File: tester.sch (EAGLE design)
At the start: 72 parts, among them IC1 ATmega8/88/168, K1 NA 05W K, M1 SP6000C-180, P1 250, P2 10k lin, Q1 BC847CSMD, Q2 BC847CSMD, Q3 BC328-40, Q4 8,000 MHz, Q5 BC847CSMD, Q9 IRFR9024, U1 LT1004CZ-2.5, U2 MCP1702-5002, U3 MCP1702-5002, U4 LM339D, U5 BCR421U, X1 NEB21R

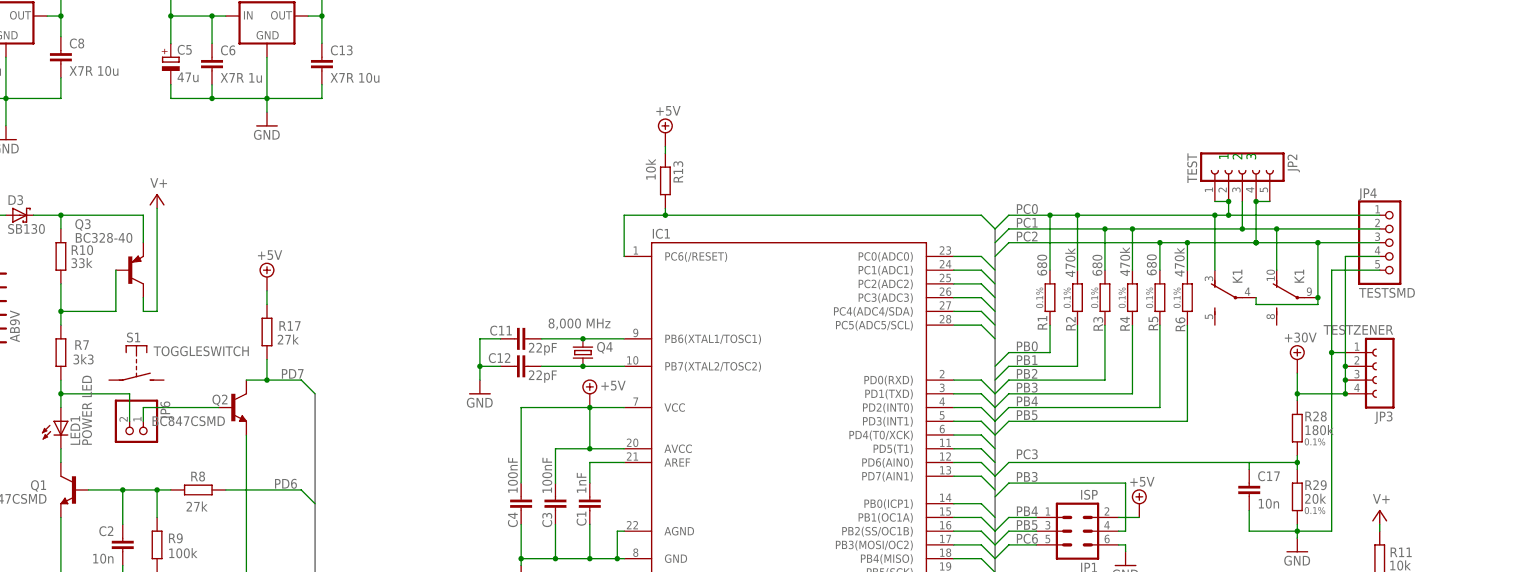
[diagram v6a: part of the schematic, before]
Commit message: rearranged top mask
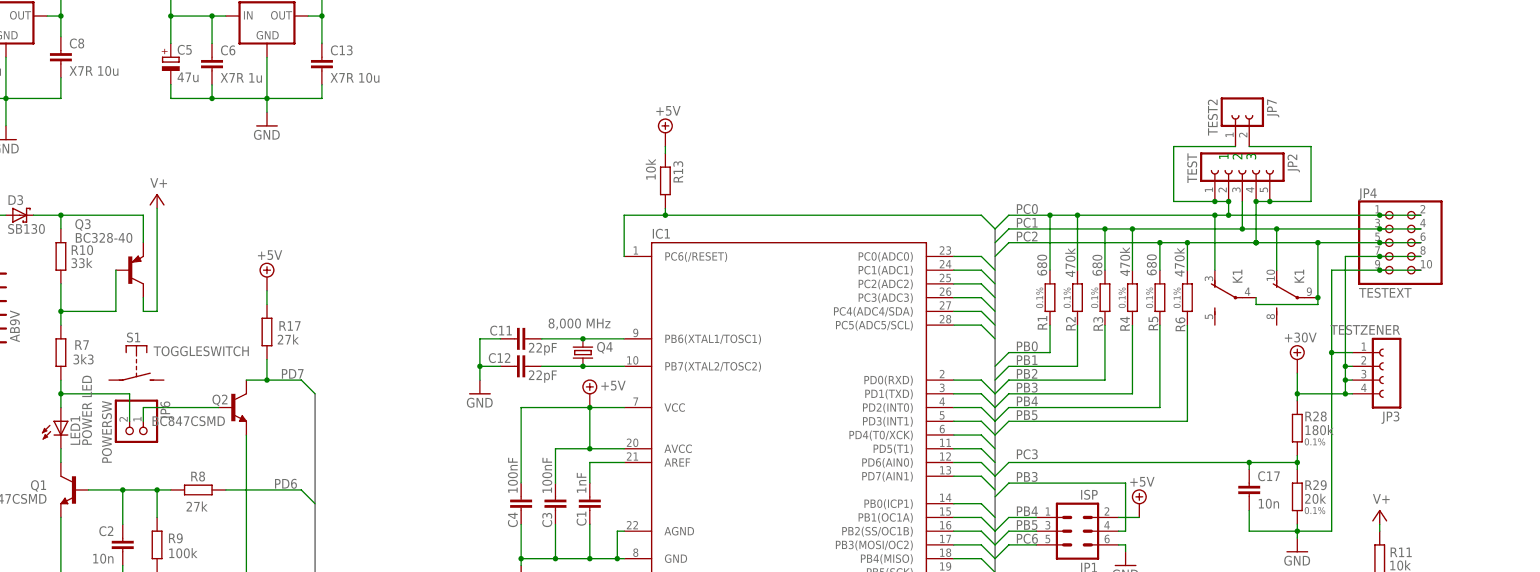
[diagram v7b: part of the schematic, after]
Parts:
- added JP7: TEST2, con-lsta:FE02-1
- JP4: value TESTSMD -> TESTEXT; device pinhead:PINHD-1X5 -> pinhead:PINHD-2X5
- JP6: value (none) -> POWERSW
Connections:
- net +30V: now also JP4.7, JP4.8; no longer JP4.4
- net GND: now also JP4.10, JP4.9; no longer JP4.5
- net PC0: now also JP4.2, JP7.1
- net PC1: now also JP4.3, JP4.4; no longer JP4.2
- net PC2: now also JP4.5, JP4.6, JP7.2; no longer JP4.3
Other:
- moved on the sheet: JP3
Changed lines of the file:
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@@
 <setting verticaltext="up"/>
 </settings>
-<grid distance="0.1" unitdist="inch" unit="mm" style="lines" multiple="1" display="yes" altdistance="0.01" altunitdist="inch" altunit="mm"/>
+<grid distance="1.27" unitdist="mm" unit="mm" style="lines" multiple="1" display="yes" altdistance="635" altunitdist="mic" altunit="mic"/>
 <layers>
 <layer number="1" name="Top" color="4" fill="1" visible="no" active="no"/>
@@
 <part name="R16" library="resistor" deviceset="R-EU_" device="R0603" value="2k2"/>
 <part name="U1" library="reference" deviceset="LM329*" device="Z" technology="D" value="LT1004CZ-2.5"/>
-<part name="JP4" library="pinhead" deviceset="PINHD-1X5" device="" value="TESTSMD">
+<part name="JP4" library="pinhead" deviceset="PINHD-2X5" device="" value="TESTEXT">
 <attribute name="REICHELT" value="AW 226/20"/>
 </part>
@@
 <part name="M1" library="strapubox" deviceset="SP6000" device="C-180" value="SP6000C-180"/>
 <part name="S1" library="external" deviceset="TOGGLESWITCH" device=""/>
-<part name="JP6" library="pinhead" deviceset="PINHD-1X2" device=""/>
+<part name="JP6" library="pinhead" deviceset="PINHD-1X2" device="" value="POWERSW"/>
 <part name="PLATINENSAMMLER" library="Platinensammler" deviceset="LP_NUMBER" device="08_SILK_TOP"/>
+<part name="JP7" library="con-lsta" deviceset="FE02-1" device="" value="TEST2"/>
 </parts>
 <sheets>
@@
 <instance part="SUPPLY2" gate="+24V" x="294.64" y="181.61"/>
 <instance part="GND7" gate="1" x="294.64" y="146.05"/>
-<instance part="JP3" gate="G$1" x="311.15" y="179.07" rot="R180"/>
+<instance part="JP3" gate="G$1" x="312.42" y="179.07" rot="R180"/>
 <instance part="D1" gate="G$1" x="288.29" y="101.6" rot="R90"/>
 <instance part="U5" gate="G$1" x="129.54" y="66.04"/>
@@
 <instance part="JP6" gate="G$1" x="78.74" y="167.64" rot="R270"/>
 <instance part="PLATINENSAMMLER" gate="G$1" x="351.79" y="248.92"/>
+<instance part="JP7" gate="G$1" x="284.48" y="228.6" rot="R270"/>
 </instances>
 <busses>
@@
 <wire x1="300.99" y1="149.86" x2="300.99" y2="182.88" width="0.1524" layer="91"/>
 <pinref part="JP3" gate="G$1" pin="1"/>
-<wire x1="300.99" y1="182.88" x2="303.53" y2="182.88" width="0.1524" layer="91"/>
+<wire x1="300.99" y1="182.88" x2="304.8" y2="182.88" width="0.1524" layer="91"/>
 <junction x="300.99" y="182.88"/>
-<pinref part="JP4" gate="A" pin="5"/>
+<pinref part="JP4" gate="A" pin="9"/>
 <wire x1="309.88" y1="198.12" x2="300.99" y2="198.12" width="0.1524" layer="91"/>
 <wire x1="300.99" y1="198.12" x2="300.99" y2="182.88" width="0.1524" layer="91"/>
+<pinref part="JP4" gate="A" pin="10"/>
+<wire x1="317.5" y1="198.12" x2="309.88" y2="198.12" width="0.1524" layer="91"/>
+<junction x="309.88" y="198.12"/>
 </segment>
 <segment>
@@
 <wire x1="279.4" y1="198.12" x2="279.4" y2="208.28" width="0.1524" layer="91"/>
 <junction x="279.4" y="208.28"/>
+<wire x1="279.4" y1="210.82" x2="271.78" y2="210.82" width="0.1524" layer="91"/>
+<junction x="279.4" y="210.82"/>
+<wire x1="271.78" y1="210.82" x2="271.78" y2="220.98" width="0.1524" layer="91"/>
+<pinref part="JP4" gate="A" pin="2"/>
+<wire x1="309.88" y1="208.28" x2="317.5" y2="208.28" width="0.1524" layer="91"/>
+<junction x="309.88" y="208.28"/>
+<pinref part="JP7" gate="G$1" pin="1"/>
+<wire x1="271.78" y1="220.98" x2="283.21" y2="220.98" width="0.1524" layer="91"/>
 </segment>
 </net>
@@
 <pinref part="JP2" gate="G$1" pin="3"/>
 <wire x1="284.48" y1="205.74" x2="284.48" y2="210.82" width="0.1524" layer="91"/>
-<pinref part="JP4" gate="A" pin="2"/>
+<pinref part="JP4" gate="A" pin="3"/>
 <wire x1="309.88" y1="205.74" x2="290.83" y2="205.74" width="0.1524" layer="91"/>
 <junction x="284.48" y="205.74"/>
@@
 <wire x1="290.83" y1="198.12" x2="290.83" y2="205.74" width="0.1524" layer="91"/>
 <junction x="290.83" y="205.74"/>
+<pinref part="JP4" gate="A" pin="4"/>
+<wire x1="317.5" y1="205.74" x2="309.88" y2="205.74" width="0.1524" layer="91"/>
+<junction x="309.88" y="205.74"/>
 </segment>
 </net>
@@
 <junction x="287.02" y="203.2"/>
 <junction x="287.02" y="203.2"/>
-<pinref part="JP4" gate="A" pin="3"/>
+<pinref part="JP4" gate="A" pin="5"/>
 <wire x1="309.88" y1="203.2" x2="298.45" y2="203.2" width="0.1524" layer="91"/>
 <pinref part="K1" gate="2" pin="P"/>
@@
 <junction x="298.45" y="203.2"/>
 <junction x="298.45" y="193.04"/>
+<wire x1="289.56" y1="210.82" x2="297.18" y2="210.82" width="0.1524" layer="91"/>
+<junction x="289.56" y="210.82"/>
+<wire x1="297.18" y1="210.82" x2="297.18" y2="220.98" width="0.1524" layer="91"/>
+<pinref part="JP4" gate="A" pin="6"/>
+<wire x1="317.5" y1="203.2" x2="309.88" y2="203.2" width="0.1524" layer="91"/>
+<junction x="309.88" y="203.2"/>
+<pinref part="JP7" gate="G$1" pin="2"/>
+<wire x1="285.75" y1="220.98" x2="297.18" y2="220.98" width="0.1524" layer="91"/>
 </segment>
 </net>
@@
 <junction x="294.64" y="162.56"/>
 <label x="242.57" y="163.195" size="1.778" layer="95"/>
+<junction x="285.75" y="162.56"/>
 </segment>
 </net>
@@
 <pinref part="R28" gate="G$1" pin="2"/>
 <wire x1="294.64" y1="175.26" x2="303.53" y2="175.26" width="0.1524" layer="91"/>
+<wire x1="303.53" y1="175.26" x2="304.8" y2="175.26" width="0.1524" layer="91"/>
 <wire x1="294.64" y1="173.99" x2="294.64" y2="175.26" width="0.1524" layer="91"/>
 <junction x="294.64" y="175.26"/>
 <pinref part="SUPPLY2" gate="+24V" pin="+24V"/>
 <pinref part="JP3" gate="G$1" pin="3"/>
-<wire x1="303.53" y1="175.26" x2="303.53" y2="177.8" width="0.1524" layer="91"/>
-<wire x1="303.53" y1="177.8" x2="303.53" y2="180.34" width="0.1524" layer="91"/>
-<junction x="303.53" y="177.8"/>
 <pinref part="JP3" gate="G$1" pin="2"/>
 <pinref part="JP3" gate="G$1" pin="4"/>
+<pinref part="JP4" gate="A" pin="7"/>
+<wire x1="309.88" y1="200.66" x2="303.53" y2="200.66" width="0.1524" layer="91"/>
+<pinref part="JP4" gate="A" pin="8"/>
+<wire x1="317.5" y1="200.66" x2="309.88" y2="200.66" width="0.1524" layer="91"/>
+<junction x="309.88" y="200.66"/>
+<wire x1="303.53" y1="175.26" x2="303.53" y2="177.8" width="0.1524" layer="91"/>
 <junction x="303.53" y="175.26"/>
+<wire x1="303.53" y1="177.8" x2="303.53" y2="180.34" width="0.1524" layer="91"/>
 <wire x1="303.53" y1="180.34" x2="303.53" y2="200.66" width="0.1524" layer="91"/>
-<pinref part="JP4" gate="A" pin="4"/>
-<wire x1="309.88" y1="200.66" x2="303.53" y2="200.66" width="0.1524" layer="91"/>
+<wire x1="304.8" y1="180.34" x2="303.53" y2="180.34" width="0.1524" layer="91"/>
 <junction x="303.53" y="180.34"/>
-</segment>
-</net>
+<wire x1="304.8" y1="177.8" x2="303.53" y2="177.8" width="0.1524" layer="91"/>
+<junction x="303.53" y="177.8"/>
+</segment>
+</net>

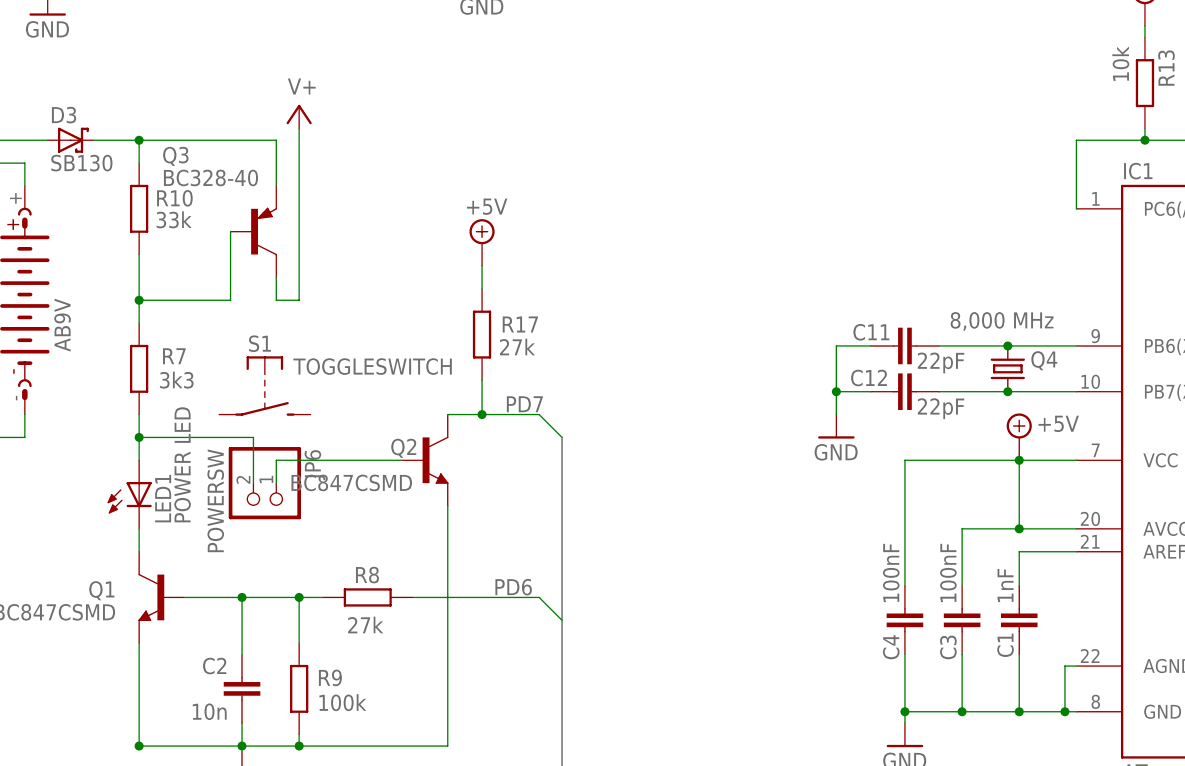
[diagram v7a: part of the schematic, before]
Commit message: cleaned up some capacitor values, changed P2 to available pinout type
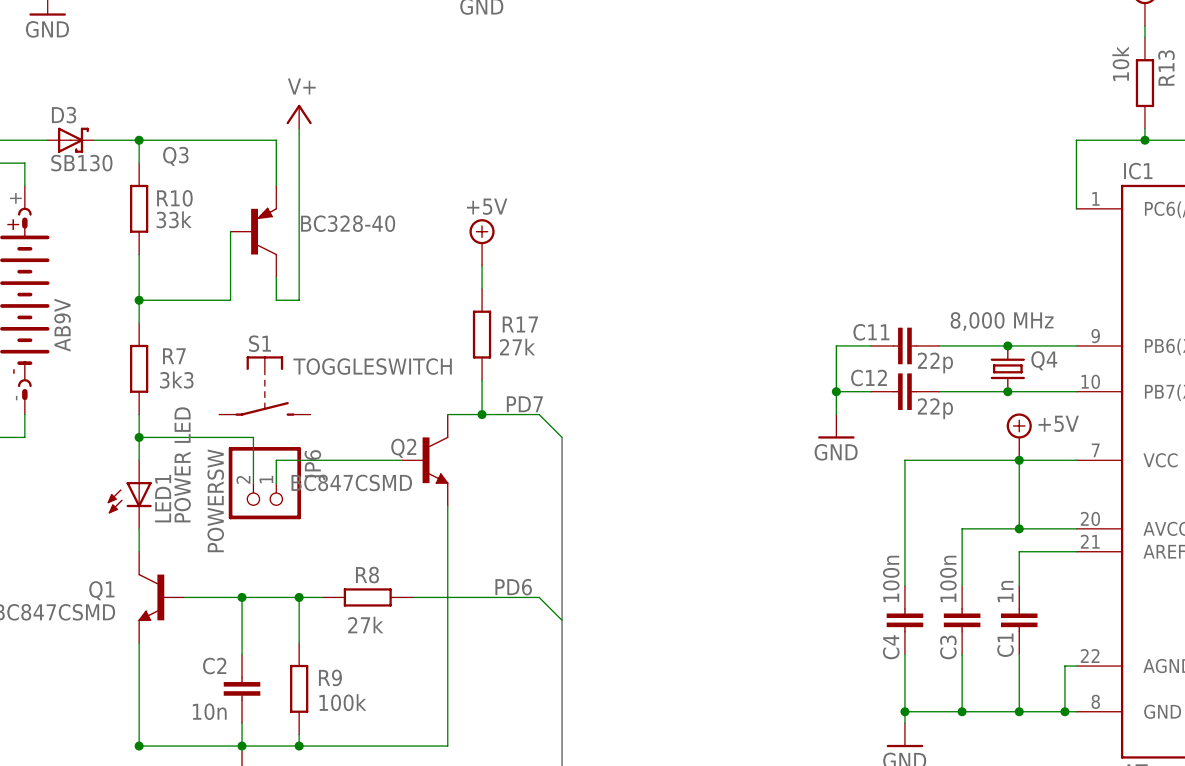
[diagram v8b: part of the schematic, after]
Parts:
- C1: value 1nF -> 1n
- C11, C12: value 22pF -> 22p
- C3, C4: value 100nF -> 100n
- D3: device markus:SCHOTTKY-DIODE_3-10 -> markus:SCHOTTKY-DIODE_RAD3-5-A
- P2: device pot:TRIM_EU-S75P -> pot:TRIM_EU-CA9V
